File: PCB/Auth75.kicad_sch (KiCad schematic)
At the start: 209 parts, among them CN1 S2B-PH-SM4-TB, Q1 MMBT3904-C20526, Q2 MMBT3904-C20526, Q3 MMBT3904-C20526, Q4 SS8550_C8542, Q5 FS8205A_C2830320, SW1 EC11E15244G1, U1 RASPBERRY PI PICO 2W, U2 SL2.1S, U3 DW01A_C351410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

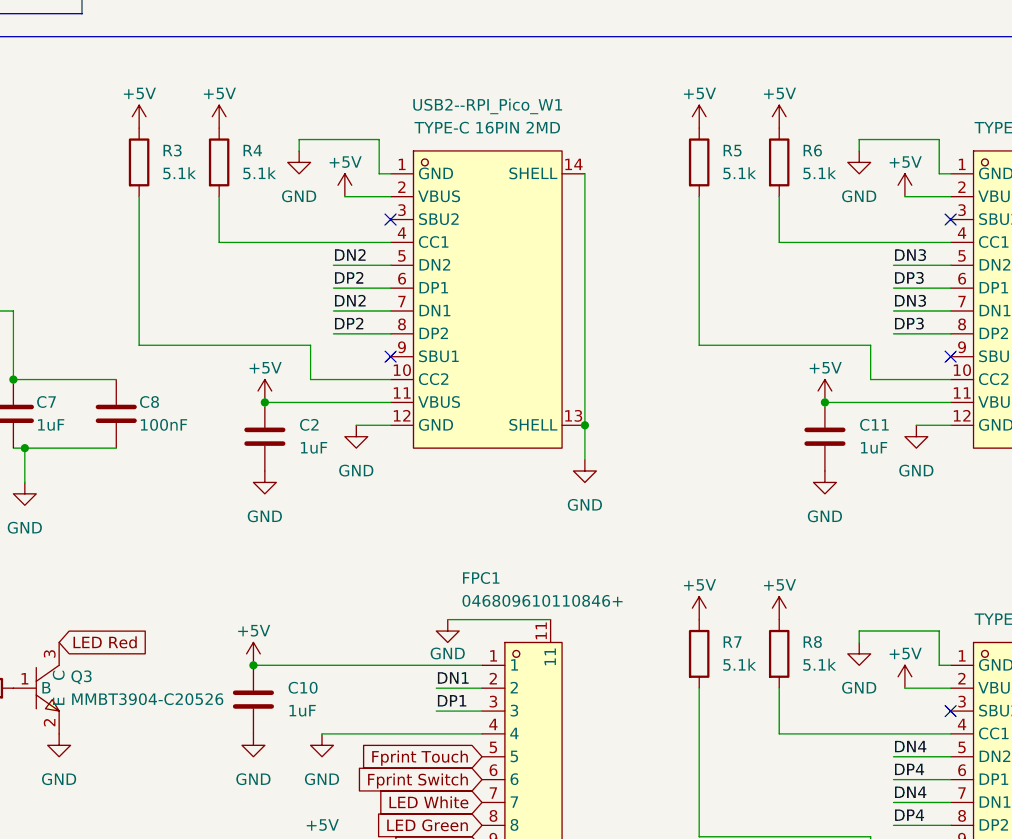
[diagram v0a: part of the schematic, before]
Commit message: 56k resis for pull up
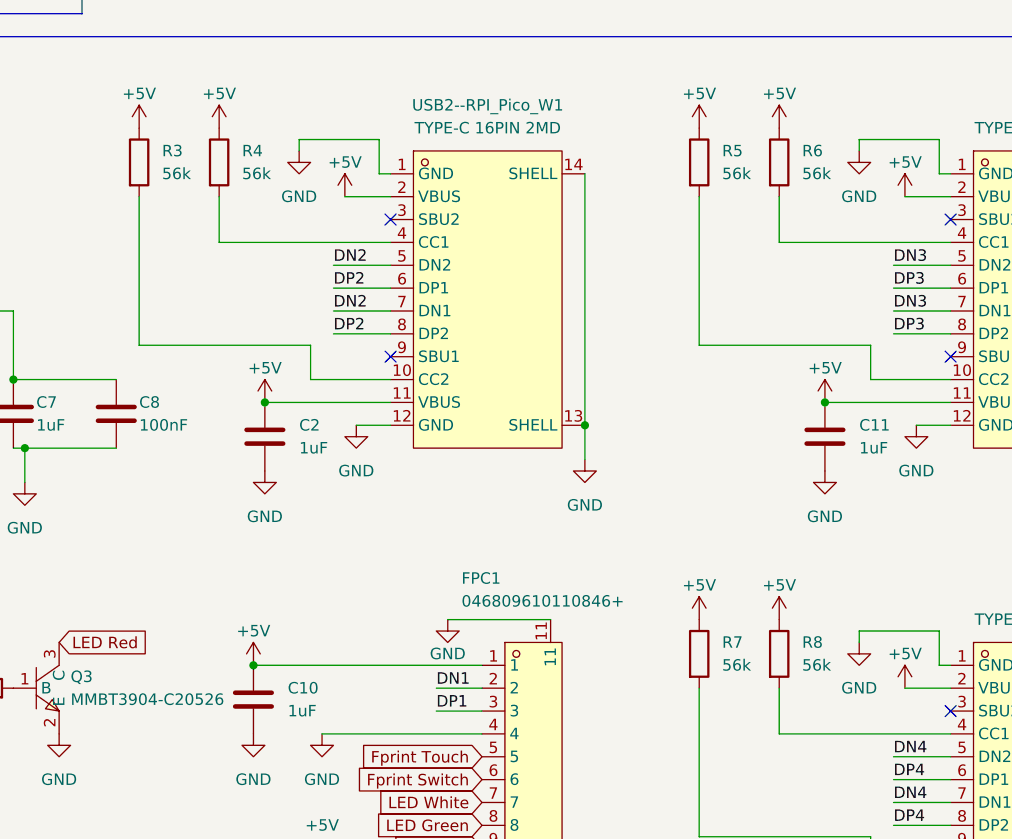
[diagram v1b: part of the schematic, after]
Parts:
- R3, R4, R5, R6, R7, R8: value 5.1k -> 56k; LCSC Part C23186 -> C23206
